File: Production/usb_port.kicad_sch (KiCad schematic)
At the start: 105 parts, among them J401 TYPE-C 16PCB1.6 IP68, Q401 PGQ04N070, Q402 PGQ04N070, Q403 AO3401A, Q404 AO3401A, Q405 AO3400A, Q406 AO3400A, Q407 PGQ04N070, Q408 PGQ04N070, U401 TPS25751DREFR, U402 M24512-DFMC6TG, U403 BQ25756RRVR, U404 TPS62933DRLR, U405 TPD4S201TRGRRQ1

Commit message: Production schematic P0: C443/C543 polymer -> 22u 25V 1206 (cap sims P3)
Each port's PP5V is its own TPS62933 (dedicated supply), so USB PD cSrcBulk
(10 uF min) applies rather than cSrcBulkShared (120 uF). PP5V output is now
3 x CL31A226KAHNNNE (~33 uF effective) + C407. Notes and README updated;
netlist check passes, ERC clean.

Co-Authored-By: Claude Opus 5.5 <noreply@anthropic.com>
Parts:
- C443: value 100u 35V -> 22u 25V; footprint Capacitor_SMD:CP_Elec_6.3x7.7 -> Capacitor_SMD:C_1206_3216Metric; symbol Device:C_Polarized -> Device:C; LCSC C5246554 -> C12891; MPN Honor Elec HV1V107M0607PZ (polymer) -> CL31A226KAHNNNE; Notes PP5V bulk: USB PD cSrcBulkShared needs 120 uF: 100 uF polym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 -> PP5V bulk, third 22 uF 1206 with C441/C442 (about 33 uF eff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
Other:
- note added: "PP5V SUPPLY TPS62933 (1.2 MHz, 5.16 V, 3 x 22u out) - 5 V source + VCONN"
- note removed: "PP5V SUPPLY TPS62933 (1.2 MHz, 5.16 V) - 5 V source + VCONN"
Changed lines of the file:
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@@
 		(comment 3 "P0: dev board rev A8 stripped by Production/tools/make_production.py; not reviewed")
 	)
-	(text "PP5V SUPPLY  TPS62933 (1.2 MHz, 5.16 V)  - 5 V source + VCONN"
+	(text "PP5V SUPPLY  TPS62933 (1.2 MHz, 5.16 V, 3 x 22u out)  - 5 V source + VCONN"
 		(exclude_from_sim no)
 		(at 40.64 186.69 0)
@@
 		)
 	)
-	(text "NOTES  (this sheet is used twice: USB Port 1 = 4xx, USB Port 2 = 5xx)\n1. Address straps are on the root sheet: port 1 ADCIN1 = LDO_3V3, ADCIN2 = GND (0x20);\n   port 2 ADCIN1 = ADCIN2 = GND (0x21). Both are SafeMode (TPS25751 table 8-6).\n2. Unused TPS25751 GPIOs (0, 1, 2, 11) tied to GND per datasheet (KiCad ERC flags this; expected).\n   Never configure them as outputs.\n3. CC and SBU are protected by U405 (TPD4S201, below); C401/C402 (220 pF) on the controller side.\n   D+ and D- are tied together at the connector (net DPDN_DCP: passive BC1.2 DCP); the TPS25751 does no BC1.2.\n   Liquid detection (TI fig. 9-8): GPIO4/5 read SBU1/2 through U405 (TPD4S201: CC and SBU OVP + ESD);\n   GPIO6 = liquid_pmos_control (LIQ_PU), GPIO7 = liquid_nmos_control (LIQ_PD) in the TPS25751 configuration.\n   U405 FLT -> GPIO3 = Fault_Input_Event (SBU_FLT, R441): an SBU short to VBUS forces error recovery.\n   R442/R443 hold the liquid-detect FETs off while GPIO6/7 are Hi-Z.\n   D401 = TVS2200 flat clamp on VBUS (28 V at 40 A 8/20 us; TI's pick for the TPS25751).\n4. Kelvin-route ACP/ACN from R424 and SRP/SRN from R427; filter parts at the IC.\n5. Two MLCCs of each bulk bank plus C430/C438 at the FETs; the bulk caps (C421 polymer, C432 hybrid polymer) and remaining MLCCs\n   one row back. Polymer carries the bulk (no DC-bias loss), MLCCs carry the switching-frequency ripple.\n   Battery side is 2 x 22u + hybrid (C435 removed: docs/devboard/cap-reduction-sims-2026-10-17.md, B2: 87 uF,\n   hybrid at 63 % of its ripple rating). Still on hold: C427 (USB side, polymer at 85 % in the worst reverse case)\n   and C443 -> 22u 1206 (until the TPS25751 120 uF cSrcBulkShared note is confirmed not to apply here).\n6. I2Cc pull-ups go to this TPS25751's own LDO_3V3 (TI guidance).\n7. The charger battery side is PACK_P directly; take SRN/FB from R427's pad, not from the pour.\n8. VAC is taken before R424 per TI typical application; DRV_SUP fed from REGN via R420.\n9. PPHV bulk (BQ25756 input bank) exceeds the 100 uF USB PD cSnkBulkPd: the TPS25751D sink switch soft-start limits\n   inrush (C x SS: about 125 uF effective x 0.47 V/ms max = 0.06 A at SS setting 0).\n   Set PPHV soft-start to setting 0 or 1 in the TPS25751 configuration.\n10. Diamonds are PWR_FLAGs (ERC only, no part): each sits where its rail is sourced through a passive part.\n11. CHG_INH: R417 pulls CE up to 3V3, so charging needs the MCU (DIO24) to drive CHG_INH low through R435.\n    Reset, WDT reset, the ROM bootloader or an unprogrammed MCU stop charging; CC2340 Standby keeps the pin state.\n    A dead pack (3V3 down) still charges. Keep DIS_CE_PIN = 0.\n12. Gate drive: R444-R447 10R at the FET gates with D406-D409 for fast turn-off. BTST is wired straight to its cap\n    and there are no snubbers (removed in P0 before any bring-up data: add them back if the dev board shows ringing).\n13. TP401 VBUS is a factory test pad."
+	(text "NOTES  (this sheet is used twice: USB Port 1 = 4xx, USB Port 2 = 5xx)\n1. Address straps are on the root sheet: port 1 ADCIN1 = LDO_3V3, ADCIN2 = GND (0x20);\n   port 2 ADCIN1 = ADCIN2 = GND (0x21). Both are SafeMode (TPS25751 table 8-6).\n2. Unused TPS25751 GPIOs (0, 1, 2, 11) tied to GND per datasheet (KiCad ERC flags this; expected).\n   Never configure them as outputs.\n3. CC and SBU are protected by U405 (TPD4S201, below); C401/C402 (220 pF) on the controller side.\n   D+ and D- are tied together at the connector (net DPDN_DCP: passive BC1.2 DCP); the TPS25751 does no BC1.2.\n   Liquid detection (TI fig. 9-8): GPIO4/5 read SBU1/2 through U405 (TPD4S201: CC and SBU OVP + ESD);\n   GPIO6 = liquid_pmos_control (LIQ_PU), GPIO7 = liquid_nmos_control (LIQ_PD) in the TPS25751 configuration.\n   U405 FLT -> GPIO3 = Fault_Input_Event (SBU_FLT, R441): an SBU short to VBUS forces error recovery.\n   R442/R443 hold the liquid-detect FETs off while GPIO6/7 are Hi-Z.\n   D401 = TVS2200 flat clamp on VBUS (28 V at 40 A 8/20 us; TI's pick for the TPS25751).\n4. Kelvin-route ACP/ACN from R424 and SRP/SRN from R427; filter parts at the IC.\n5. Two MLCCs of each bulk bank plus C430/C438 at the FETs; the bulk caps (C421 polymer, C432 hybrid polymer) and remaining MLCCs\n   one row back. Polymer carries the bulk (no DC-bias loss), MLCCs carry the switching-frequency ripple.\n   Battery side is 2 x 22u + hybrid (C435 removed: docs/devboard/cap-reduction-sims-2026-10-17.md, B2: 87 uF,\n   hybrid at 63 % of its ripple rating). Still on hold: C427 (USB side, polymer at 85 % in the worst reverse case).\n6. I2Cc pull-ups go to this TPS25751's own LDO_3V3 (TI guidance).\n7. The charger battery side is PACK_P directly; take SRN/FB from R427's pad, not from the pour.\n8. VAC is taken before R424 per TI typical application; DRV_SUP fed from REGN via R420.\n9. PPHV bulk (BQ25756 input bank) exceeds the 100 uF USB PD cSnkBulkPd: the TPS25751D sink switch soft-start limits\n   inrush (C x SS: about 125 uF effective x 0.47 V/ms max = 0.06 A at SS setting 0).\n   Set PPHV soft-start to setting 0 or 1 in the TPS25751 configuration.\n10. Diamonds are PWR_FLAGs (ERC only, no part): each sits where its rail is sourced through a passive part.\n11. CHG_INH: R417 pulls CE up to 3V3, so charging needs the MCU (DIO24) to drive CHG_INH low through R435.\n    Reset, WDT reset, the ROM bootloader or an unprogrammed MCU stop charging; CC2340 Standby keeps the pin state.\n    A dead pack (3V3 down) still charges. Keep DIS_CE_PIN = 0.\n12. Gate drive: R444-R447 10R at the FET gates with D406-D409 for fast turn-off. BTST is wired straight to its cap\n    and there are no snubbers (removed in P0 before any bring-up data: add them back if the dev board shows ringing).\n13. TP401 VBUS is a factory test pad.\n14. PP5V output: C441-C443 3 x 22u 1206 (about 33 uF effective) plus C407 10u at the PP5V pin. Each port's PP5V is\n    its own TPS62933, a dedicated supply: USB PD cSrcBulk (10 uF min) applies, not the 120 uF cSrcBulkShared the\n    TPS25751 table cites. Estimated 0.5 -> 3 A step undershoot about 190 mV (cap sims P3); measure it on the dev board."
 		(exclude_from_sim no)
 		(at 299.72 368.3 0)
@@
 	)
 	(symbol
-		(lib_id "Device:C_Polarized")
+		(lib_id "Device:C")
 		(at 157.48 207.01 0)
 		(unit 1)
@@
 			)
 		)
-		(property "Value" "100u 35V"
+		(property "Value" "22u 25V"
 			(at 157.48 201.27 0)
 			(show_name no)
@@
 			)
 		)
-		(property "Footprint" "Capacitor_SMD:CP_Elec_6.3x7.7"
+		(property "Footprint" "Capacitor_SMD:C_1206_3216Metric"
 			(at 158.445 203.2 0)
 			(hide yes)
@@
 			)
 		)
-		(property "Notes" "PP5V bulk: USB PD cSrcBulkShared needs 120 uF: 100 uF polymer (no DC-bias loss) + C441/C442 2 x 22 uF. Same part as C421 since 2026-10-15 (was a 220 uF 16 V polymer) to save a JLC extended-part fee"
+		(property "Notes" "PP5V bulk, third 22 uF 1206 with C441/C442 (about 33 uF effective at 5.16 V; was a 100 uF polymer on the dev board). Each port's PP5V is a dedicated supply, so USB PD cSrcBulk (10 uF min) applies, not cSrcBulkShared (120 uF): docs/devboard/cap-reduction-sims-2026-10-17.md, P3"
 			(at 0 0 0)
 			(hide yes)
@@
 			)
 		)
-		(property "LCSC" "C5246554"
+		(property "LCSC" "C12891"
 			(at 157.48 207.01 0)
 			(hide yes)
@@
 			)
 		)
-		(property "MPN" "Honor Elec HV1V107M0607PZ (polymer)"
+		(property "MPN" "CL31A226KAHNNNE"
 			(at 157.48 207.01 0)
 			(hide yes)

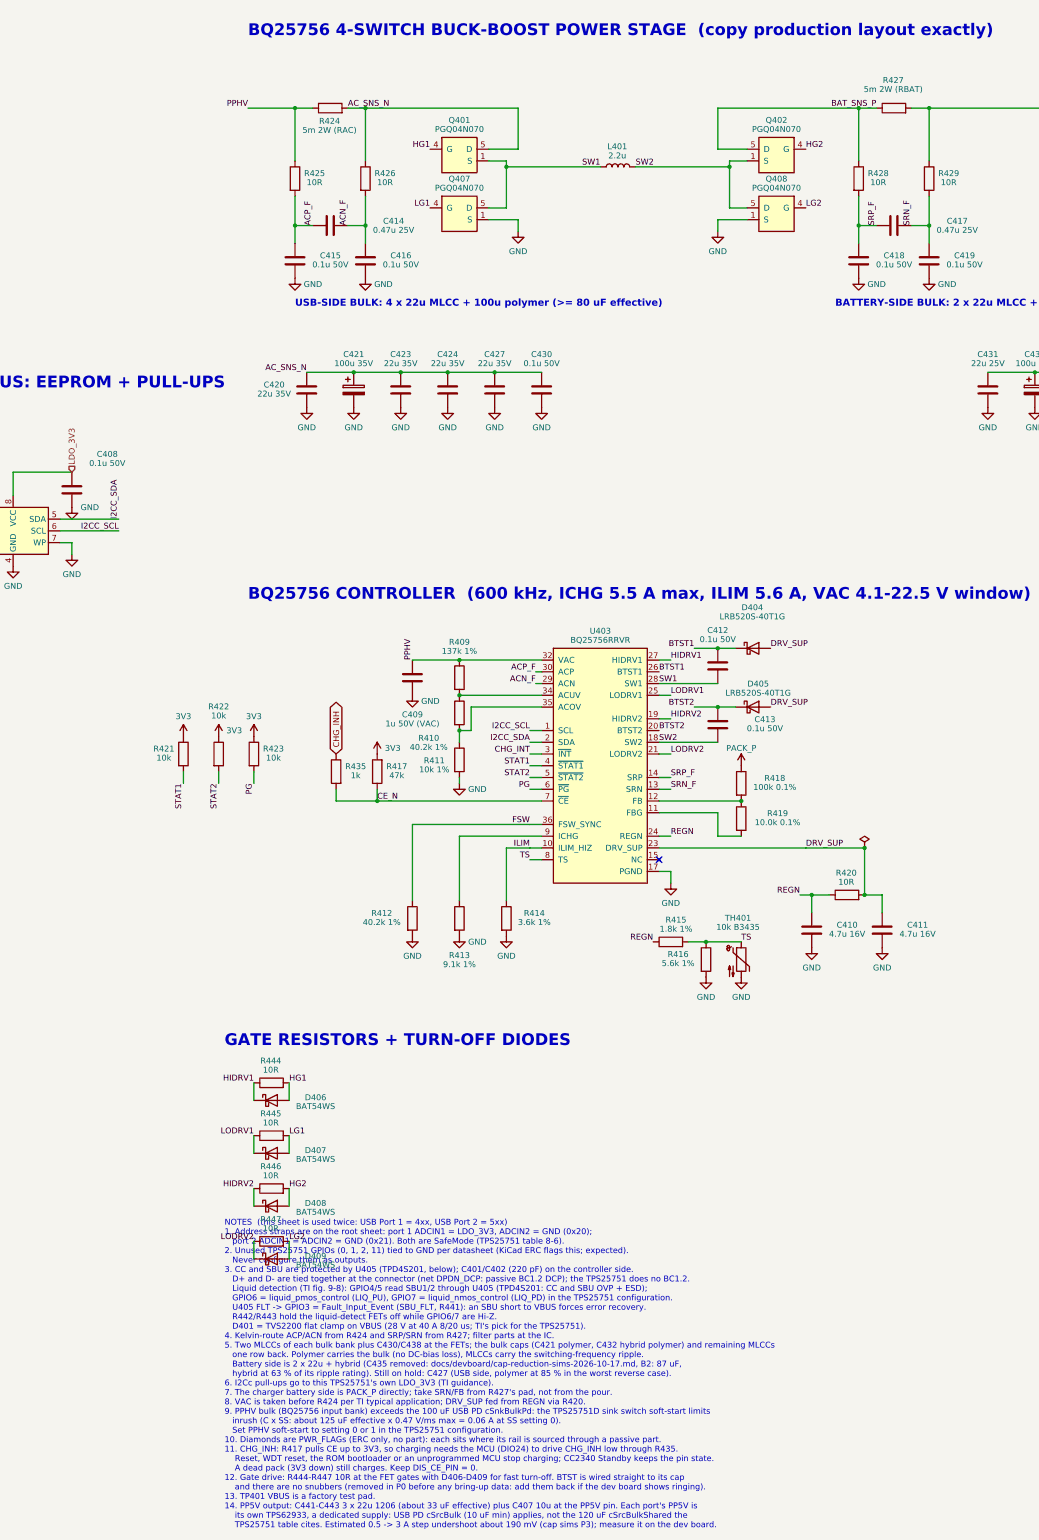
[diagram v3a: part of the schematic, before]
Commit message: Production schematic P0: passive downsizing (-432 mm2 courtyard, -16 %)
Extended parts and 0201 allowed on production (0201 only where both nets stay
<= 5.5 V). Charger inductor 10x10 -> Coilank APS0730M2R2F; 0603 R -> 0402;
low-voltage R/C -> 0201; RAC 0805, RBAT 1206, gauge shunt 1206; R101-R104
0402; BAT54 SOD-882; REGN/filter/SS caps 0402; NTC 0402. Bulk polymers and
TPS25751/TPS62933 caps kept (leakage, derating). New APS0730 footprint is
written by make_production.py. Netlist check passes; ERC clean.

Co-Authored-By: Claude Opus 5.5 <noreply@anthropic.com>
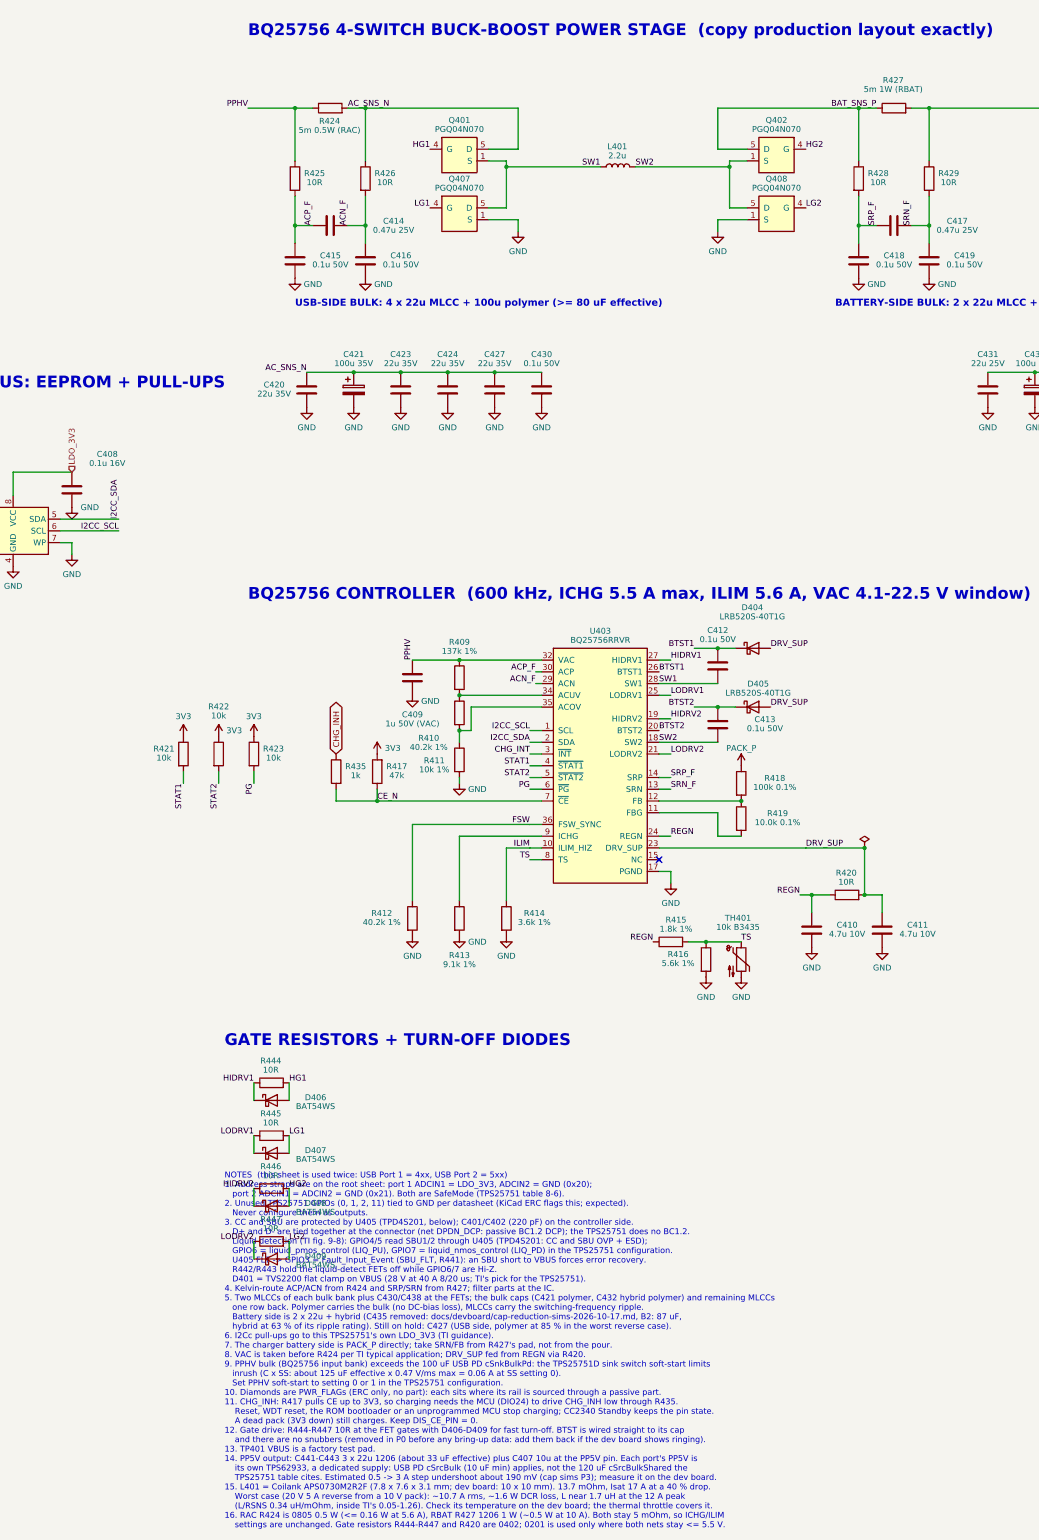
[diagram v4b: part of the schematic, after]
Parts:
- C408: value 0.1u 50V -> 0.1u 16V; footprint Capacitor_SMD:C_0402_1005Metric -> Capacitor_SMD:C_0201_0603Metric; LCSC C307331 -> C307380; MPN CL05B104KB54PNC -> CL03A104KO3NNNC
- C410, C411: value 4.7u 16V -> 4.7u 10V; footprint Capacitor_SMD:C_0603_1608Metric -> Capacitor_SMD:C_0402_1005Metric; LCSC C19666 -> C23733; MPN CL10A475KO8NNNC -> CL05A475MP5NRNC
- C414, C417: footprint Capacitor_SMD:C_0603_1608Metric -> Capacitor_SMD:C_0402_1005Metric; LCSC C1623 -> C92361; MPN CL10B474KA8NNNC -> CL05A474KA5NNNC
- C439: footprint Capacitor_SMD:C_0603_1608Metric -> Capacitor_SMD:C_0402_1005Metric; LCSC C21117 -> C7419416; MPN CL10B333KB8NNNC -> FCC0402B333K500AT
- D406, D407, D408, D409: footprint Diode_SMD:D_SOD-323 -> Diode_SMD:D_SOD-882; LCSC C7502694 -> C549279; MPN BAT54WS (R+O) -> BAT54L,315 (Nexperia)
- L401: footprint Inductor_SMD:L_Changjiang_FXL1040 -> MonolithDev:L_Coilank_APS0730; LCSC C149591 -> C49261221; MPN SMMS1040-2R2M (SXN) -> APS0730M2R2F (Coilank)
- R402, R403: footprint Resistor_SMD:R_0402_1005Metric -> Resistor_SMD:R_0201_0603Metric; LCSC C25890 -> C270350; MPN 0402WGF3301TCE -> 0201WMF3301TEE
- R404, R421, R422, R423: footprint Resistor_SMD:R_0402_1005Metric -> Resistor_SMD:R_0201_0603Metric; LCSC C25744 -> C473048; MPN 0402WGF1002TCE -> 0201WMF1002TEE
- R410: footprint Resistor_SMD:R_0603_1608Metric -> Resistor_SMD:R_0402_1005Metric; LCSC C12447 -> C25893; MPN 0603WAF4022T5E -> 0402WGF4022TCE
- R412: footprint Resistor_SMD:R_0603_1608Metric -> Resistor_SMD:R_0201_0603Metric; LCSC C12447 -> C423536; MPN 0603WAF4022T5E -> 0201WMF4022TEE
- R413: footprint Resistor_SMD:R_0603_1608Metric -> Resistor_SMD:R_0402_1005Metric; LCSC C23260 -> C25926; MPN 0603WAF9101T5E -> 0402WGF9101TCE
- R414: footprint Resistor_SMD:R_0603_1608Metric -> Resistor_SMD:R_0402_1005Metric; LCSC C22980 -> C25891; MPN 0603WAF3601T5E -> 0402WGF3601TCE
- R415: footprint Resistor_SMD:R_0603_1608Metric -> Resistor_SMD:R_0402_1005Metric; LCSC C4177 -> C25871; MPN 0603WAF1801T5E -> 0402WGF1801TCE
- R416: footprint Resistor_SMD:R_0603_1608Metric -> Resistor_SMD:R_0402_1005Metric; LCSC C23189 -> C25908; MPN 0603WAF5601T5E -> 0402WGF5601TCE
- R417: footprint Resistor_SMD:R_0402_1005Metric -> Resistor_SMD:R_0201_0603Metric; LCSC C25792 -> C270345; MPN 0402WGF4702TCE -> 0201WMF4702TEE
- R420, R444, R445, R446, R447: footprint Resistor_SMD:R_0603_1608Metric -> Resistor_SMD:R_0402_1005Metric; LCSC C22859 -> C25077; MPN 0603WAF100JT5E -> 0402WGF100JTCE
- R424: value 5m 2W (RAC) -> 5m 0.5W (RAC); footprint Resistor_SMD:R_2010_5025Metric -> Resistor_SMD:R_0805_2012Metric; LCSC C7256567 -> C728267; MPN PA2010FKE470R005Z -> PA0805FRE470R005L
- R427: value 5m 2W (RBAT) -> 5m 1W (RBAT); footprint Resistor_SMD:R_2010_5025Metric -> Resistor_SMD:R_1206_3216Metric; LCSC C7256567 -> C252653; MPN PA2010FKE470R005Z -> MA120610FR005MZ (50 ppm)
- R432, R441, R442, R443: footprint Resistor_SMD:R_0402_1005Metric -> Resistor_SMD:R_0201_0603Metric; LCSC C25741 -> C270364; MPN 0402WGF1003TCE -> 0201WMF1003TEE
- R433: footprint Resistor_SMD:R_0603_1608Metric -> Resistor_SMD:R_0402_1005Metric; LCSC C25808 -> C25750; MPN 0603WAF1203T5E -> 0402WGF1203TCE
- R435: footprint Resistor_SMD:R_0402_1005Metric -> Resistor_SMD:R_0201_0603Metric; LCSC C11702 -> C270365; MPN 0402WGF1001TCE -> 0201WMF1001TEE
- TH401: footprint Resistor_SMD:R_0603_1608Metric -> Resistor_SMD:R_0402_1005Metric; LCSC C13564 -> C77131; MPN NCP18XH103F03RB -> NCP15XH103F03RC

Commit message: Production schematic P0: direct gate drive, one shared PACK_P hybrid
R444-R447 -> copper, D406-D409 removed (gates driven directly). Battery-side
banks of both chargers, both TPS62933 inputs and the pack modelled as one bus
(tools/pack_bus_sims.py): C432/C532 hybrids -> one shared C208 on PACK_P,
C445/C545 removed. 99 uF effective (>= 80 uF C_OUT), worst part 44 %, damping
20 dB. Courtyard 2221 -> 2104 mm2. Netlist check passes; ERC clean.

Co-Authored-By: Claude Opus 5.5 <noreply@anthropic.com>
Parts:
- removed C432: 100u 25V, Capacitor_SMD:CP_Elec_6.3x7.7, symbol Device:C_Polarized
- removed C445: 10u 50V, Capacitor_SMD:C_1206_3216Metric, symbol Device:C
- removed D406, D407, D408, D409: BAT54WS, Diode_SMD:D_SOD-882, symbol Device:D_Schottky
- removed R444, R445, R446, R447: 10R, Resistor_SMD:R_0402_1005Metric, symbol Device:R
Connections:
- net HG1 is gone; now on net HIDRV1: Q401.4 (G)
- net HG2 is gone; now on net HIDRV2: Q402.4 (G)
- net LG1 is gone; now on net LODRV1: Q407.4 (G)
- net LG2 is gone; now on net LODRV2: Q408.4 (G)
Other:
- note added: "BATTERY-SIDE LOCAL: 2 x 22u MLCC; bulk is the shared PACK_P hybrid C208 (3V3 Rail sheet)"
- note removed: "BATTERY-SIDE BULK: 2 x 22u MLCC + 100u hybrid polymer (87 uF effective, >= 80 uF)"
- note removed: "GATE RESISTORS + TURN-OFF DIODES"

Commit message: Production schematic P0: remove liquid detection
Q403-Q406, R436-R439, R442/R443 (both ports) removed. TPS25751 GPIO4-7 tied to
GND (unused), TPD4S201 system-side SBU pins no-connect, FLT -> GPIO3 kept.
make_production.py gains PIN_ACTIONS; check_netlist.py accepts the intended
NET_MOVES. Dual-FET option checked and not applied (README). Netlist check
passes; ERC: only expected warnings.

Co-Authored-By: Claude Opus 5.5 <noreply@anthropic.com>
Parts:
- removed Q403, Q404: AO3401A, Package_TO_SOT_SMD:SOT-23, symbol Transistor_FET:Q_PMOS_GSD
- removed Q405, Q406: AO3400A, Package_TO_SOT_SMD:SOT-23, symbol Transistor_FET:Q_NMOS_GSD
- removed R436, R437: 100k, Resistor_SMD:R_0402_1005Metric, symbol Device:R
- removed R438, R439: 1M, Resistor_SMD:R_0402_1005Metric, symbol Device:R
- removed R442, R443: 100k, Resistor_SMD:R_0201_0603Metric, symbol Device:R
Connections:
- net LIQ_PD is gone; now on net GND: U401.36 (GPIO7)
- net LIQ_PU is gone; now on net GND: U401.37 (GPIO6)
- net GND: now also U401.26 (GPIO4), U401.27 (GPIO5)
- net SBU1_SNS: no longer names the net of U405.15 (SBU1)
- net SBU1_SNS: no longer U401.26 (GPIO4)
- net SBU2_SNS: no longer names the net of U405.14 (SBU2)
- net SBU2_SNS: no longer U401.27 (GPIO5)
- no-connect marks 1 -> 3
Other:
- note added: "CC/SBU PROTECTION (TPD4S201)"
- note added: "NOTES (this sheet is used twice: USB Port 1 = 4xx, USB Port 2 = 5xx) 1. Address straps are on the root sheet: port 1 ADCIN1 = LDO_3V3, ADCIN2 = GND (0x20); port 2 ADCIN1 = ADCIN2 = GND (0x21). Both are SafeMode (TPS25751 table 8-6). 2. Unused TPS25751 GPIOs (0, 1, 2, 4-7, 11) tied to GND per datasheet (KiCad ERC flags this; expected). Never configure them as outputs. 3. CC and SBU are protected b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"
- note removed: "CC/SBU PROTECTION (TPD4S201) + LIQUID DETECTION"
- note removed: "NOTES (this sheet is used twice: USB Port 1 = 4xx, USB Port 2 = 5xx) 1. Address straps are on the root sheet: port 1 ADCIN1 = LDO_3V3, ADCIN2 = GND (0x20); port 2 ADCIN1 = ADCIN2 = GND (0x21). Both are SafeMode (TPS25751 table 8-6). 2. Unused TPS25751 GPIOs (0, 1, 2, 11) tied to GND per datasheet (KiCad ERC flags this; expected). Never configure them as outputs. 3. CC and SBU are protected by U40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"
